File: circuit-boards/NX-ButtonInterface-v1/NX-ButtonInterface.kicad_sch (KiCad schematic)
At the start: 3 parts, among them J1 NX CONTROL & UART, J2 NX-BUTTON, J4 POWER LED

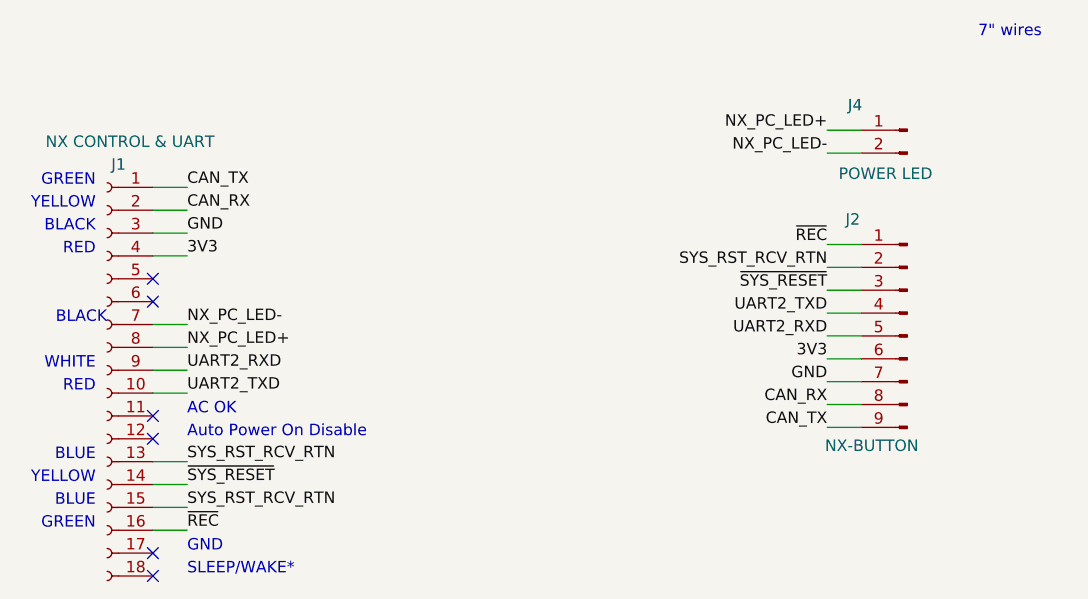
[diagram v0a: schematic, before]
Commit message: Update NX-J401 and NX Button Interface boards
Signed-off-by: Scott Berman <scott.berman@bluerivertech.com>
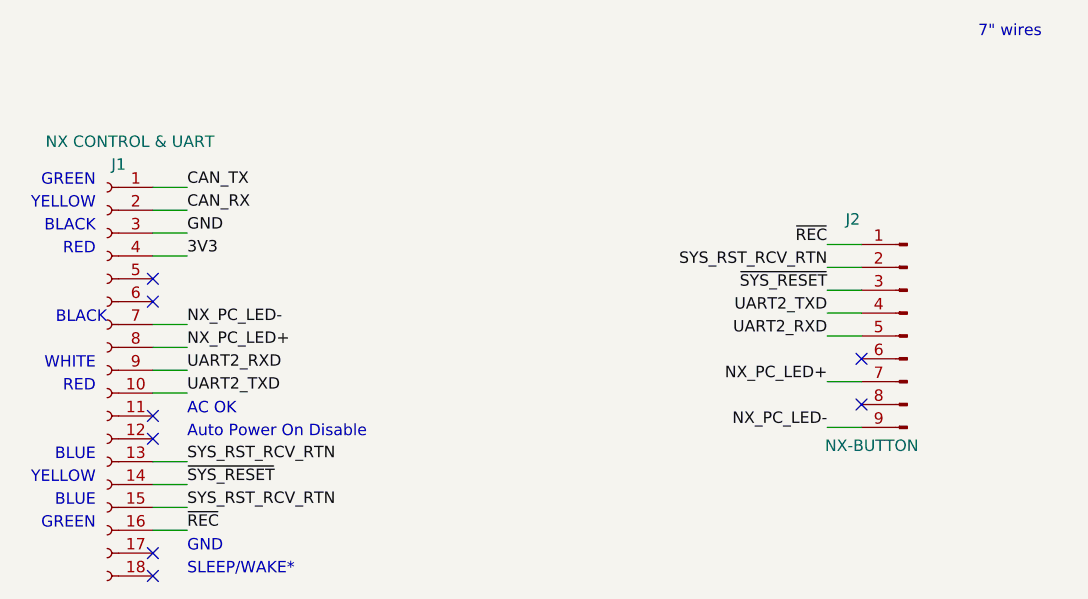
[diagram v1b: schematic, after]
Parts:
- removed J4: POWER LED, NX-ButtonInterface:2-pin-solder-pads, symbol Connector:Conn_01x02_Pin
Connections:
- net 3V3: no longer J2.6 (Pin_6)
- net CAN_RX: no longer J2.8 (Pin_8)
- net CAN_TX: no longer J2.9 (Pin_9)
- net GND: no longer J2.7 (Pin_7)
- net NX_PC_LED+: now also J2.7 (Pin_7)
- net NX_PC_LED-: now also J2.9 (Pin_9)
- no-connect marks 6 -> 8
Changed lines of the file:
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@@
 	(title_block
 		(title "NX Button Interface V1")
-		(date "2025-01-13")
+		(date "2025-01-15")
 		(rev "1")
 	)
@@
 	)
 	(no_connect
+		(at 170.18 96.52)
+	)
+	(no_connect
 		(at 91.44 82.55)
 	)
@@
 		(at 91.44 97.79)
 	)
+	(no_connect
+		(at 170.18 91.44)
+	)
 	(wire
 		(pts
@@
 	(wire
 		(pts
-			(xy 166.37 96.52) (xy 170.18 96.52)
-		)
-		(stroke
-			(width 0)
-			(type default)
-		)
-	)
-	(wire
-		(pts
 			(xy 166.37 99.06) (xy 170.18 99.06)
 		)
@@
 	(wire
 		(pts
-			(xy 166.37 66.04) (xy 170.18 66.04)
-		)
-		(stroke
-			(width 0)
-			(type default)
-		)
-	)
-	(wire
-		(pts
 			(xy 166.37 78.74) (xy 170.18 78.74)
 		)
@@
 	(wire
 		(pts
-			(xy 166.37 91.44) (xy 170.18 91.44)
-		)
-		(stroke
-			(width 0)
-			(type default)
-		)
-	)
-	(wire
-		(pts
 			(xy 95.25 87.63) (xy 91.44 87.63)
 		)
@@
 		)
 	)
-	(wire
-		(pts
-			(xy 166.37 68.58) (xy 170.18 68.58)
-		)
-		(stroke
-			(width 0)
-			(type default)
-		)
-	)
 	(text "RED"
 		(exclude_from_sim no)
@@
 			)
 			(justify left bottom)
-		)
-	)
-	(label "NX_PC_LED-"
-		(at 166.37 68.58 180)
-		(fields_autoplaced yes)
-		(effects
-			(font
-				(size 1.27 1.27)
-			)
-			(justify right bottom)
 		)
 	)
 	(label "UART2_TXD"
 		(at 166.37 86.36 180)
-		(fields_autoplaced yes)
 		(effects
 			(font
@@
 	(label "~{SYS_RESET}"
 		(at 95.25 105.41 0)
-		(fields_autoplaced yes)
 		(effects
 			(font
@@
 	(label "CAN_TX"
 		(at 95.25 72.39 0)
-		(fields_autoplaced yes)
 		(effects
 			(font
@@
 	(label "GND"
 		(at 95.25 77.47 0)
-		(fields_autoplaced yes)
-		(effects
-			(font
-				(size 1.27 1.27)
-			)
-			(justify left bottom)
-		)
-	)
-	(label "3V3"
-		(at 166.37 91.44 180)
-		(fields_autoplaced yes)
-		(effects
-			(font
-				(size 1.27 1.27)
-			)
-			(justify right bottom)
+		(effects
+			(font
+				(size 1.27 1.27)
+			)
+			(justify left bottom)
 		)
 	)
 	(label "~{REC}"
 		(at 95.25 110.49 0)
-		(fields_autoplaced yes)
 		(effects
 			(font
@@
 	(label "UART2_RXD"
 		(at 166.37 88.9 180)
-		(fields_autoplaced yes)
 		(effects
 			(font
@@
 	(label "NX_PC_LED+"
 		(at 95.25 90.17 0)
-		(fields_autoplaced yes)
 		(effects
 			(font
@@
 	(label "SYS_RST_RCV_RTN"
 		(at 166.37 81.28 180)
-		(fields_autoplaced yes)
-		(effects
-			(font
-				(size 1.27 1.27)
-			)
-			(justify right bottom)
-		)
-	)
-	(label "CAN_TX"
-		(at 166.37 99.06 180)
-		(fields_autoplaced yes)
 		(effects
 			(font
@@
 	(label "CAN_RX"
 		(at 95.25 74.93 0)
-		(fields_autoplaced yes)
-		(effects
-			(font
-				(size 1.27 1.27)
-			)
-			(justify left bottom)
-		)
-	)
-	(label "CAN_RX"
-		(at 166.37 96.52 180)
-		(fields_autoplaced yes)
-		(effects
-			(font
-				(size 1.27 1.27)
-			)
-			(justify right bottom)
+		(effects
+			(font
+				(size 1.27 1.27)
+			)
+			(justify left bottom)
 		)
 	)
 	(label "~{SYS_RESET}"
 		(at 166.37 83.82 180)
-		(fields_autoplaced yes)
+		(effects
+			(font
+				(size 1.27 1.27)
+			)
+			(justify right bottom)
+		)
+	)
+	(label "NX_PC_LED+"
+		(at 166.37 93.98 180)
 		(effects
 			(font
@@
 	(label "3V3"
 		(at 95.25 80.01 0)
-		(fields_autoplaced yes)
-		(effects
-			(font
-				(size 1.27 1.27)
-			)
-			(justify left bottom)
-		)
-	)
-	(label "GND"
-		(at 166.37 93.98 180)
-		(fields_autoplaced yes)
-		(effects
-			(font
-				(size 1.27 1.27)
-			)
-			(justify right bottom)
-		)
-	)
-	(label "NX_PC_LED+"
-		(at 166.37 66.04 180)
-		(fields_autoplaced yes)
-		(effects
-			(font
-				(size 1.27 1.27)
-			)
-			(justify right bottom)
+		(effects
+			(font
+				(size 1.27 1.27)
+			)
+			(justify left bottom)
 		)
 	)
 	(label "~{REC}"
 		(at 166.37 78.74 180)
-		(fields_autoplaced yes)
 		(effects
 			(font
@@
 	(label "SYS_RST_RCV_RTN"
 		(at 95.25 107.95 0)
-		(fields_autoplaced yes)
 		(effects
 			(font
@@
 	(label "UART2_RXD"
 		(at 95.25 92.71 0)
-		(fields_autoplaced yes)
-		(effects
-			(font
-				(size 1.27 1.27)
-			)
-			(justify left bottom)
+		(effects
+			(font
+				(size 1.27 1.27)
+			)
+			(justify left bottom)
+		)
+	)
+	(label "NX_PC_LED-"
+		(at 166.37 99.06 180)
+		(effects
+			(font
+				(size 1.27 1.27)
+			)
+			(justify right bottom)
 		)
 	)
 	(label "UART2_TXD"
 		(at 95.25 95.25 0)
-		(fields_autoplaced yes)
 		(effects
 			(font
@@
 	(label "NX_PC_LED-"
 		(at 95.25 87.63 0)
-		(fields_autoplaced yes)
 		(effects
 			(font
@@
 	(label "SYS_RST_RCV_RTN"
 		(at 95.25 102.87 0)
-		(fields_autoplaced yes)
 		(effects
 			(font
@@
 					(unit 1)
 				)
-			)
-		)
-	)
-	(symbol
-		(lib_id "Connector:Conn_01x02_Pin")
-		(at 175.26 66.04 0)
-		(mirror y)
-		(unit 1)
-		(exclude_from_sim no)
-		(in_bom yes)
-		(on_board yes)
-		(dnp no)
-		(property "Reference" "J4"
-			(at 168.656 63.246 0)
-			(effects
-				(font
-					(size 1.27 1.27)
-				)
-				(justify right)
-			)
-		)
-		(property "Value" "POWER LED"
-			(at 167.64 70.866 0)
-			(effects
-				(font
-					(size 1.27 1.27)
-				)
-				(justify right)
-			)
-		)
-		(property "Footprint" "NX-ButtonInterface:2-pin-solder-pads"
-			(at 175.26 66.04 0)
-			(effects
-				(font
-					(size 1.27 1.27)
-				)
-				(hide yes)
-			)
-		)
-		(property "Datasheet" "~"
-			(at 175.26 66.04 0)
-			(effects
-				(font
-					(size 1.27 1.27)
-				)
-				(hide yes)
-			)
-		)
-		(property "Description" "Generic connector, single row, 01x02, script generated"
-			(at 175.26 66.04 0)
-			(effects
-				(font
-					(size 1.27 1.27)
-				)
-				(hide yes)
-			)
-		)
-		(pin "2"
-		)
-		(pin "1"
-		)
-		(instances
-			(project ""
-				(path "/a7eb5823-c87f-41de-b6ed-af0ad18b6b3c"
-					(reference "J4")
-					(unit 1)
-				)
